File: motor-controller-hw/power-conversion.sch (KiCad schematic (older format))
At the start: 0 parts

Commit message: Added more signals to the top level diagram
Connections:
- net labels added: D_GND, GNDD, GNDPWR, PWM_Phase_AH, PWM_Phase_AL, PWM_Phase_BH, PWM_Phase_BL, PWM_Phase_CH, PWM_Phase_CL, P_GND, Phase_A_Current, Phase_A_HALFX, Phase_B_Current, Phase_B_HALFX, Phase_C_Current, Phase_C_HALFX, vBat
- wire segments 0 -> 4
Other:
- note added: "Seprate grounds for digital supply \nand power, joined in the system"
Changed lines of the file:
@@
 $Descr A4 11693 8268
 encoding utf-8
-Sheet 1 7
+Sheet 7 7
 Title ""
 Date ""
@@
 Comment4 ""
 $EndDescr
+Text HLabel 1550 950  0    50   Input ~ 0
+PWM_Phase_AH
+Text HLabel 1550 1050 0    50   Input ~ 0
+PWM_Phase_AL
+Text HLabel 1550 1200 0    50   Input ~ 0
+PWM_Phase_BH
+Text HLabel 1550 1300 0    50   Input ~ 0
+PWM_Phase_BL
+Text HLabel 1550 1450 0    50   Input ~ 0
+PWM_Phase_CH
+Text HLabel 1550 1550 0    50   Input ~ 0
+PWM_Phase_CL
+Text HLabel 1550 1700 0    50   Output ~ 0
+Phase_A_Current
+Text HLabel 1550 1800 0    50   Output ~ 0
+Phase_B_Current
+Text HLabel 1550 1900 0    50   Output ~ 0
+Phase_C_Current
+Text HLabel 1550 2050 0    50   Output ~ 0
+Phase_A_HALFX
+Text HLabel 1550 2150 0    50   Output ~ 0
+Phase_B_HALFX
+Text HLabel 1550 2250 0    50   Output ~ 0
+Phase_C_HALFX
+Text HLabel 1550 2400 0    50   UnSpc ~ 0
+D_GND
+Text HLabel 1550 2500 0    50   UnSpc ~ 0
+P_GND
+$Comp
+L power:GNDPWR #PWR?
+U 1 1 5BBBD74A
+P 1800 2600
+F 0 "#PWR?" H 1800 2400 50  0001 C CNN
+F 1 "GNDPWR" H 1804 2446 50  0000 C CNN
+F 2 "" H 1800 2550 50  0001 C CNN
+F 3 "" H 1800 2550 50  0001 C CNN
+	1    1800 2600
+	1    0    0    -1
+$EndComp
+$Comp
+L power:GNDD #PWR?
+U 1 1 5BBBD7C0
+P 2100 2600
+F 0 "#PWR?" H 2100 2350 50  0001 C CNN
+F 1 "GNDD" H 2104 2445 50  0000 C CNN
+F 2 "" H 2100 2600 50  0001 C CNN
+F 3 "" H 2100 2600 50  0001 C CNN
+	1    2100 2600
+	1    0    0    -1
+$EndComp
+Wire Wire Line
+	1550 2400 2100 2400
+Wire Wire Line
+	2100 2400 2100 2600
+Wire Wire Line
+	1550 2500 1800 2500
+Wire Wire Line
+	1800 2500 1800 2600
+Text Notes 2400 3000 2    50   ~ 0
+Seprate grounds for digital supply \nand power, joined in the system
+Text HLabel 1550 800  0    50   Input ~ 0
+vBat
 $EndSCHEMATC

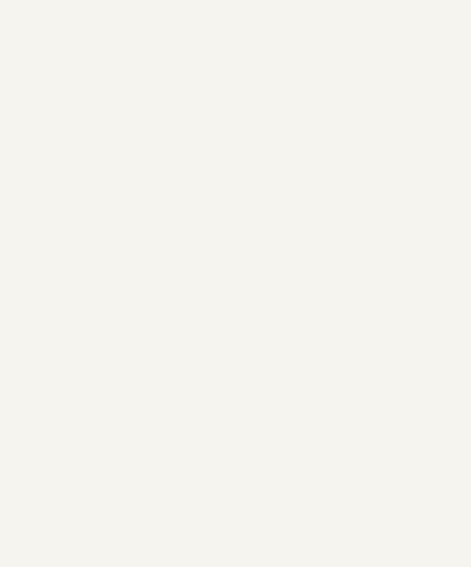
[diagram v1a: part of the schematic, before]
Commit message: added more signals and parts
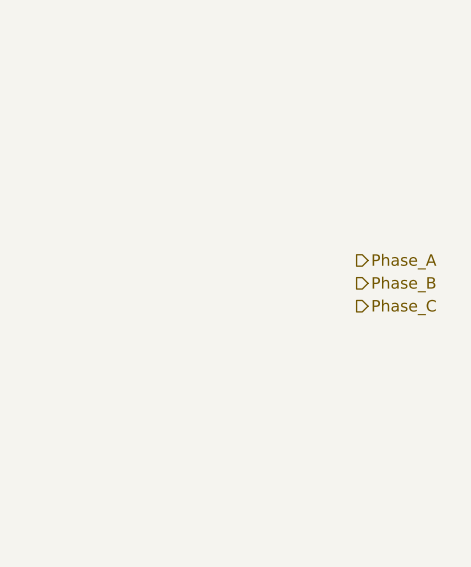
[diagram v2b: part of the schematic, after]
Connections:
- net labels added: Phase_A, Phase_B, Phase_C
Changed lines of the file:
@@
 P_GND
 $Comp
-L power:GNDPWR #PWR?
+L MotorControllerParts:GNDPWR #PWR?
 U 1 1 5BBBD74A
 P 1800 2600
@@
 $EndComp
 $Comp
-L power:GNDD #PWR?
+L MotorControllerParts:GNDD #PWR?
 U 1 1 5BBBD7C0
 P 2100 2600
@@
 Text HLabel 1550 800  0    50   Input ~ 0
 vBat
+Text HLabel 8800 1850 2    50   Output ~ 0
+Phase_A
+Text HLabel 8800 1950 2    50   Output ~ 0
+Phase_B
+Text HLabel 8800 2050 2    50   Output ~ 0
+Phase_C
 $EndSCHEMATC
